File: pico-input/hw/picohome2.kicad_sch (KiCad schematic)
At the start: 123 parts, among them J1 LVCONN, J2 LVCONN, J3 24VDC, J4 24VDC, J5 SWD, J8 Input, SW1 RESET, U1 PC817, U10 PC817, U11 PC817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

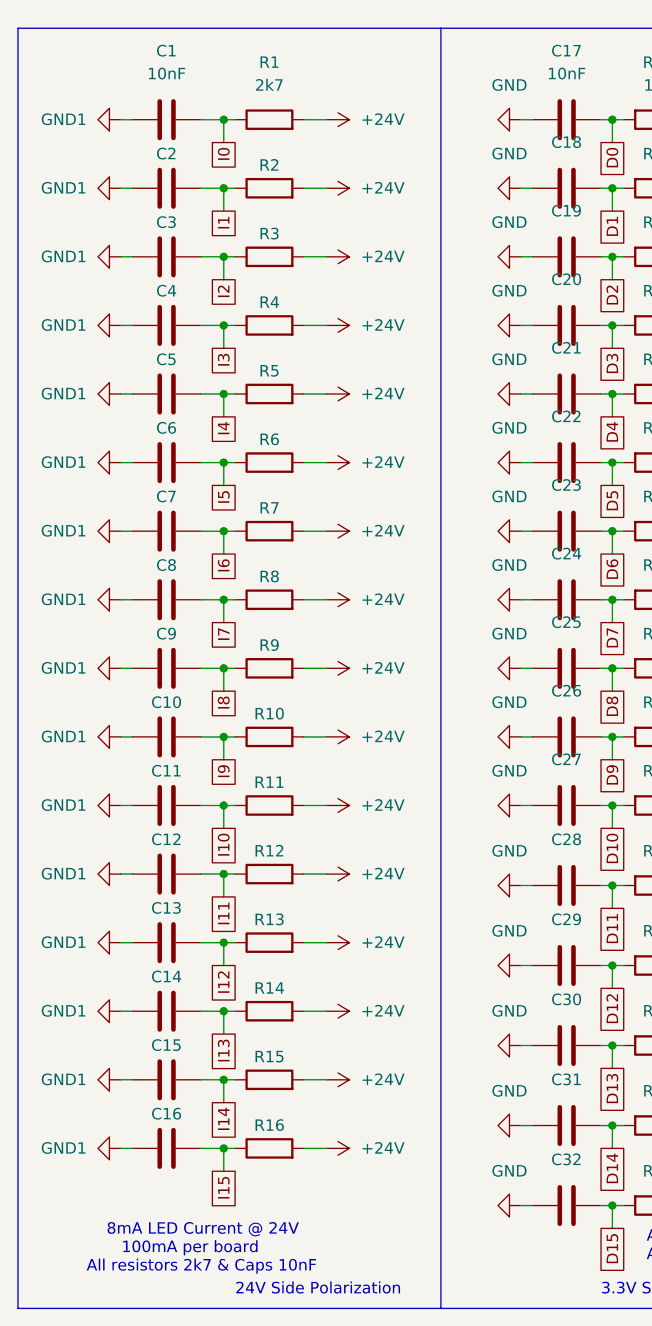
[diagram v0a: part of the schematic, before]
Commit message: Update 24V Pull-up resistors to 10k (2k7 dissipates too much heat)
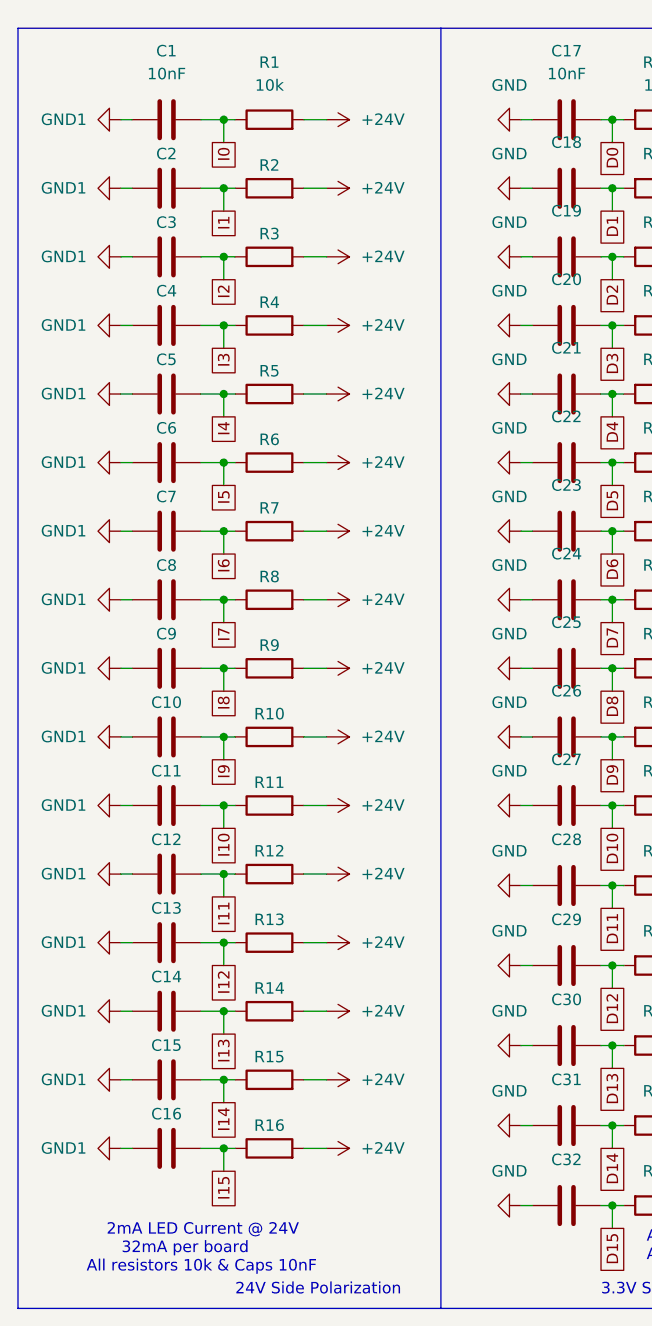
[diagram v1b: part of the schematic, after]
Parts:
- R1, R10, R11, R12, R13, R14, R15, R16, R2, R3, R4, R5, R6, R7, R8, R9: value 2k7 -> 10k
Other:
- note added: "2mA LED Current @ 24V 32mA per board All resistors 10k & Caps 10nF"
- note removed: "8mA LED Current @ 24V 100mA per board All resistors 2k7 & Caps 10nF"
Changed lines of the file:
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@@
     (stroke (width 0) (type default) (color 0 0 0 0))
   )
-  (text "    8mA LED Current @ 24V\n       100mA per board\nAll resistors 2k7 & Caps 10nF"
+  (text "    2mA LED Current @ 24V\n       32mA per board\nAll resistors 10k & Caps 10nF"
     (at 69.85 213.36 0)
     (effects (font (size 1.27 1.27)) (justify left bottom))
@@
     (in_bom yes) (on_board yes) (fields_autoplaced)
     (property "Reference" "R13" (id 0) (at 90.17 173.99 90))
-    (property "Value" "2k7" (id 1) (at 90.17 172.72 90)
+    (property "Value" "10k" (id 1) (at 90.17 172.72 90)
       (effects (font (size 1.27 1.27)) hide)
     )
@@
     (in_bom yes) (on_board yes) (fields_autoplaced)
     (property "Reference" "R15" (id 0) (at 90.17 189.23 90))
-    (property "Value" "2k7" (id 1) (at 90.17 187.96 90)
+    (property "Value" "10k" (id 1) (at 90.17 187.96 90)
       (effects (font (size 1.27 1.27)) hide)
     )
@@
     (in_bom yes) (on_board yes) (fields_autoplaced)
     (property "Reference" "R11" (id 0) (at 90.17 158.75 90))
-    (property "Value" "2k7" (id 1) (at 90.17 157.48 90)
+    (property "Value" "10k" (id 1) (at 90.17 157.48 90)
       (effects (font (size 1.27 1.27)) hide)
     )
@@
     (in_bom yes) (on_board yes) (fields_autoplaced)
     (property "Reference" "R2" (id 0) (at 90.17 90.17 90))
-    (property "Value" "2k7" (id 1) (at 90.17 88.9 90)
+    (property "Value" "10k" (id 1) (at 90.17 88.9 90)
       (effects (font (size 1.27 1.27)) hide)
     )
@@
     (in_bom yes) (on_board yes) (fields_autoplaced)
     (property "Reference" "R14" (id 0) (at 90.17 181.61 90))
-    (property "Value" "2k7" (id 1) (at 90.17 180.34 90)
+    (property "Value" "10k" (id 1) (at 90.17 180.34 90)
       (effects (font (size 1.27 1.27)) hide)
     )
@@
     (in_bom yes) (on_board yes) (fields_autoplaced)
     (property "Reference" "R12" (id 0) (at 90.17 166.37 90))
-    (property "Value" "2k7" (id 1) (at 90.17 165.1 90)
+    (property "Value" "10k" (id 1) (at 90.17 165.1 90)
       (effects (font (size 1.27 1.27)) hide)
     )
@@
     (in_bom yes) (on_board yes) (fields_autoplaced)
     (property "Reference" "R9" (id 0) (at 90.17 143.51 90))
-    (property "Value" "2k7" (id 1) (at 90.17 142.24 90)
+    (property "Value" "10k" (id 1) (at 90.17 142.24 90)
       (effects (font (size 1.27 1.27)) hide)
     )
@@
     (in_bom yes) (on_board yes) (fields_autoplaced)
     (property "Reference" "R16" (id 0) (at 90.17 196.85 90))
-    (property "Value" "2k7" (id 1) (at 90.17 195.58 90)
+    (property "Value" "10k" (id 1) (at 90.17 195.58 90)
       (effects (font (size 1.27 1.27)) hide)
     )
@@
     (in_bom yes) (on_board yes) (fields_autoplaced)
     (property "Reference" "R4" (id 0) (at 90.17 105.41 90))
-    (property "Value" "2k7" (id 1) (at 90.17 104.14 90)
+    (property "Value" "10k" (id 1) (at 90.17 104.14 90)
       (effects (font (size 1.27 1.27)) hide)
     )
@@
     (in_bom yes) (on_board yes) (fields_autoplaced)
     (property "Reference" "R1" (id 0) (at 90.17 78.74 90))
-    (property "Value" "2k7" (id 1) (at 90.17 81.28 90))
+    (property "Value" "10k" (id 1) (at 90.17 81.28 90))
     (property "Footprint" "Resistor_SMD:R_0805_2012Metric_Pad1.20x1.40mm_HandSolder" (id 2) (at 90.17 86.868 90)
       (effects (font (size 1.27 1.27)) hide)
@@
     (in_bom yes) (on_board yes) (fields_autoplaced)
     (property "Reference" "R3" (id 0) (at 90.17 97.79 90))
-    (property "Value" "2k7" (id 1) (at 90.17 96.52 90)
+    (property "Value" "10k" (id 1) (at 90.17 96.52 90)
       (effects (font (size 1.27 1.27)) hide)
     )
@@
     (in_bom yes) (on_board yes) (fields_autoplaced)
     (property "Reference" "R10" (id 0) (at 90.17 151.13 90))
-    (property "Value" "2k7" (id 1) (at 90.17 149.86 90)
+    (property "Value" "10k" (id 1) (at 90.17 149.86 90)
       (effects (font (size 1.27 1.27)) hide)
     )
@@
     (in_bom yes) (on_board yes) (fields_autoplaced)
     (property "Reference" "R7" (id 0) (at 90.17 128.27 90))
-    (property "Value" "2k7" (id 1) (at 90.17 127 90)
+    (property "Value" "10k" (id 1) (at 90.17 127 90)
       (effects (font (size 1.27 1.27)) hide)
     )
@@
     (in_bom yes) (on_board yes) (fields_autoplaced)
     (property "Reference" "R8" (id 0) (at 90.17 135.89 90))
-    (property "Value" "2k7" (id 1) (at 90.17 134.62 90)
+    (property "Value" "10k" (id 1) (at 90.17 134.62 90)
       (effects (font (size 1.27 1.27)) hide)
     )
@@
     (in_bom yes) (on_board yes) (fields_autoplaced)
     (property "Reference" "R5" (id 0) (at 90.17 113.03 90))
-    (property "Value" "2k7" (id 1) (at 90.17 111.76 90)
+    (property "Value" "10k" (id 1) (at 90.17 111.76 90)
       (effects (font (size 1.27 1.27)) hide)
     )
@@
     (in_bom yes) (on_board yes) (fields_autoplaced)
     (property "Reference" "R6" (id 0) (at 90.17 120.65 90))
-    (property "Value" "2k7" (id 1) (at 90.17 119.38 90)
+    (property "Value" "10k" (id 1) (at 90.17 119.38 90)
       (effects (font (size 1.27 1.27)) hide)
     )
@@
     )
     (path "/7af2fa37-1b02-4bc0-9ca4-2b5db21d1ac5"
-      (reference "R1") (unit 1) (value "2k7") (footprint "Resistor_SMD:R_0805_2012Metric_Pad1.20x1.40mm_HandSolder")
+      (reference "R1") (unit 1) (value "10k") (footprint "Resistor_SMD:R_0805_2012Metric_Pad1.20x1.40mm_HandSolder")
     )
     (path "/2aaec602-cd45-4bda-baa7-dbc5df70b43e"
-      (reference "R2") (unit 1) (value "2k7") (footprint "Resistor_SMD:R_0805_2012Metric_Pad1.20x1.40mm_HandSolder")
+      (reference "R2") (unit 1) (value "10k") (footprint "Resistor_SMD:R_0805_2012Metric_Pad1.20x1.40mm_HandSolder")
     )
     (path "/a33bb196-dd27-437d-b5c3-5aa9d7f3f883"
-      (reference "R3") (unit 1) (value "2k7") (footprint "Resistor_SMD:R_0805_2012Metric_Pad1.20x1.40mm_HandSolder")
+      (reference "R3") (unit 1) (value "10k") (footprint "Resistor_SMD:R_0805_2012Metric_Pad1.20x1.40mm_HandSolder")
     )
     (path "/73414ca6-8727-432a-a8b9-9dca4cda085b"
-      (reference "R4") (unit 1) (value "2k7") (footprint "Resistor_SMD:R_0805_2012Metric_Pad1.20x1.40mm_HandSolder")
+      (reference "R4") (unit 1) (value "10k") (footprint "Resistor_SMD:R_0805_2012Metric_Pad1.20x1.40mm_HandSolder")
     )
     (path "/f2789c68-01e3-4bb5-89fe-55d884b7908c"
-      (reference "R5") (unit 1) (value "2k7") (footprint "Resistor_SMD:R_0805_2012Metric_Pad1.20x1.40mm_HandSolder")
+      (reference "R5") (unit 1) (value "10k") (footprint "Resistor_SMD:R_0805_2012Metric_Pad1.20x1.40mm_HandSolder")
     )
     (path "/fa827dbf-a399-4e62-9b22-06fd5ec88df6"
-      (reference "R6") (unit 1) (value "2k7") (footprint "Resistor_SMD:R_0805_2012Metric_Pad1.20x1.40mm_HandSolder")
+      (reference "R6") (unit 1) (value "10k") (footprint "Resistor_SMD:R_0805_2012Metric_Pad1.20x1.40mm_HandSolder")
     )
     (path "/d2fd143e-5fc1-4b1e-ab4c-9337955afcda"
-      (reference "R7") (unit 1) (value "2k7") (footprint "Resistor_SMD:R_0805_2012Metric_Pad1.20x1.40mm_HandSolder")
+      (reference "R7") (unit 1) (value "10k") (footprint "Resistor_SMD:R_0805_2012Metric_Pad1.20x1.40mm_HandSolder")
     )
     (path "/eae39d3c-39ac-4eed-af7b-a2c7dc5b49cf"
-      (reference "R8") (unit 1) (value "2k7") (footprint "Resistor_SMD:R_0805_2012Metric_Pad1.20x1.40mm_HandSolder")
+      (reference "R8") (unit 1) (value "10k") (footprint "Resistor_SMD:R_0805_2012Metric_Pad1.20x1.40mm_HandSolder")
     )
     (path "/5373a763-b34c-42b0-99ca-4b9fc0e10215"
-      (reference "R9") (unit 1) (value "2k7") (footprint "Resistor_SMD:R_0805_2012Metric_Pad1.20x1.40mm_HandSolder")
+      (reference "R9") (unit 1) (value "10k") (footprint "Resistor_SMD:R_0805_2012Metric_Pad1.20x1.40mm_HandSolder")
     )
     (path "/b83b791d-2ca9-4ad8-85ce-d4fd7a6d0ab9"
-      (reference "R10") (unit 1) (value "2k7") (footprint "Resistor_SMD:R_0805_2012Metric_Pad1.20x1.40mm_HandSolder")
+      (reference "R10") (unit 1) (value "10k") (footprint "Resistor_SMD:R_0805_2012Metric_Pad1.20x1.40mm_HandSolder")
     )
     (path "/07413d1d-89e5-4888-a35e-7061fdef2289"
-      (reference "R11") (unit 1) (value "2k7") (footprint "Resistor_SMD:R_0805_2012Metric_Pad1.20x1.40mm_HandSolder")
+      (reference "R11") (unit 1) (value "10k") (footprint "Resistor_SMD:R_0805_2012Metric_Pad1.20x1.40mm_HandSolder")
     )
     (path "/4b535a78-d33e-45f4-8345-2b9007d7c709"
-      (reference "R12") (unit 1) (value "2k7") (footprint "Resistor_SMD:R_0805_2012Metric_Pad1.20x1.40mm_HandSolder")
+      (reference "R12") (unit 1) (value "10k") (footprint "Resistor_SMD:R_0805_2012Metric_Pad1.20x1.40mm_HandSolder")
     )
     (path "/007459da-5977-4579-84dd-e811ff987fcc"
-      (reference "R13") (unit 1) (value "2k7") (footprint "Resistor_SMD:R_0805_2012Metric_Pad1.20x1.40mm_HandSolder")
+      (reference "R13") (unit 1) (value "10k") (footprint "Resistor_SMD:R_0805_2012Metric_Pad1.20x1.40mm_HandSolder")
     )
     (path "/2bcbed60-284c-4e6e-9847-fcaf0bae7485"
-      (reference "R14") (unit 1) (value "2k7") (footprint "Resistor_SMD:R_0805_2012Metric_Pad1.20x1.40mm_HandSolder")
+      (reference "R14") (unit 1) (value "10k") (footprint "Resistor_SMD:R_0805_2012Metric_Pad1.20x1.40mm_HandSolder")
     )
     (path "/03a7af78-e1e3-4fc9-9d62-cc83b9f3c30b"
-      (reference "R15") (unit 1) (value "2k7") (footprint "Resistor_SMD:R_0805_2012Metric_Pad1.20x1.40mm_HandSolder")
+      (reference "R15") (unit 1) (value "10k") (footprint "Resistor_SMD:R_0805_2012Metric_Pad1.20x1.40mm_HandSolder")
     )
     (path "/60ff497c-ef13-4382-8835-255c1cca058d"
-      (reference "R16") (unit 1) (value "2k7") (footprint "Resistor_SMD:R_0805_2012Metric_Pad1.20x1.40mm_HandSolder")
+      (reference "R16") (unit 1) (value "10k") (footprint "Resistor_SMD:R_0805_2012Metric_Pad1.20x1.40mm_HandSolder")
     )
     (path "/089491c1-1a8f-426a-b487-d8cac7e5d334"
